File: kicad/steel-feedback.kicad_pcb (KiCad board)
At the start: 2 copper layers, 220 x 130 mm, 154 parts, among them J1 AudioJack2_SwitchT, J2 AudioJack2_SwitchT, J4 AudioJack2_SwitchT, J5 AudioJack2_SwitchT, J6 AudioJack2_SwitchT, J7 AudioJack2_SwitchT, J8 Jack-DC, Q1 2N3904, Q2 2N3906, Q3 2N3906, SW1 SW_SPDT, SW2 SW_SPDT, SW3 SW_SPDT, U10 TL072, U11 TL072, U12 TL072, U13 TL072, U2 LM13700, U3 LM13700, U4 TL072, U5 TL072, U6 LM386, U7 NE5534, U8 TL072, U9 ICL7660

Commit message: Tweaking values now that build is in progress
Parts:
- removed LS1: Speaker, KK254_Horizontal:Molex_KK-254_1x02_P2.54mm_Horizontal
- removed MK1: Piezo, KK254_Horizontal:Molex_KK-254_1x02_P2.54mm_Horizontal
- added H1: MountingHole_Pad, MountingHole:MountingHole_3.2mm_M3_Pad, F.Cu at (34.0, 34.0)
- added H2: MountingHole_Pad, MountingHole:MountingHole_3.2mm_M3_Pad, F.Cu at (246.0, 34.0)
- added H3: MountingHole_Pad, MountingHole:MountingHole_3.2mm_M3_Pad, F.Cu at (34.0, 156.0)
- added H4: MountingHole_Pad, MountingHole:MountingHole_3.2mm_M3_Pad, F.Cu at (246.0, 156.0)
- added J10: Conn_01x02, Rumblesan_Connectors:Molex_KK-254_22-05-7028_1x02_P2.54mm_Horizontal, F.Cu at (147.8, 139.7)
- added J3: Conn_01x03_Pin, Rumblesan_Connectors:Molex_KK-254_22-05-7038_1x03_P2.54mm_Horizontal, F.Cu at (215.1, 101.9)
- added J9: Conn_01x02, Rumblesan_Connectors:Molex_KK-254_22-05-7028_1x02_P2.54mm_Horizontal, F.Cu at (93.5, 139.8)
- C1, C2, C3: value 100pF -> 150pF
- C35: value 20pF -> 22pF
- C41: value 33nF -> 47nF
- C9: value 220uF -> 100uF
- J8: value Jack-DC -> Conn_01x02; footprint KK254_Horizontal:Molex_KK-254_1x02_P2.54mm_Horizontal -> Rumblesan_Connectors:Molex_KK-254_22-05-7028_1x02_P2.54mm_Horizontal
- R25: value 56k -> 68k
- R29: value 2k2 -> 2k
- moved C25 17.2 mm to (166.6, 133.9)
- moved C11 12.2 mm to (146.8, 113.5)
- moved C34 6.78 mm to (165.1, 145.8), turned to -90 degrees
- moved C9 6.61 mm to (86.9, 145.5), turned to 0 degrees
- moved C20 6.10 mm to (166.6, 138.7), turned to -90 degrees
- moved D3 5.24 mm to (180.1, 149.1)
- moved C10 3.81 mm to (141.7, 140.0)
- moved C7 1.80 mm to (83.3, 133.1)
- moved C29 1.78 mm to (196.8, 106.9), turned to 90 degrees
- moved J8 0.12 mm to (184.9, 140.0)
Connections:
- D3 pad 1: VCC -> Net-(D3-K)
- D3 pad 2: GND -> VCC
- SW1 pad 1: VCC -> Net-(D3-K)
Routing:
- net VEE: track 481.2 -> 496.3 mm
- net Net-(C11-Pad1): track 36.5 -> 48.7 mm
- net FEEDBACK_AUDIO: track 150.2 -> 139.5 mm
- net Net-(C41-Pad1): track 44.3 -> 52.5 mm
- net VCC: track 590.3 -> 597.7 mm, vias 0 -> 2
- net Net-(D3-K): track 0.00 -> 6.91 mm
- net Net-(U6-BYPASS): track 7.19 -> 9.07 mm
- net Net-(D1-A): track 47.8 -> 49.3 mm
- net Net-(C10-Pad1): track 5.50 -> 6.24 mm
- net GNDD: vias 1 -> 0
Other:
- board text added: "+V"
- board text added: "-V"
- board text added: "0V"
- board text added: "Debug Power"
- board text added: "Feedback Attenuvert"
- board text added: "Feedback CV"
- board text added: "Feedback Gain"
- board text added: "Frequency"
- board text added: "Frequency Attenuvert"
- board text added: "Frequency CV"
- board text added: "In Phase"
- board text added: "Input 1"
- board text added: "Input 2"
- board text added: "Invert"
- board text added: "Low Cut"
- board text added: "Off"
- board text added: "On"
- board text added: "Output 1"
- board text added: "Output 2"
- board text added: "Pickup"
- board text added: "Pickup Gain"
- board text added: "Plate Drive"
- board text added: "Resonance"

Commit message: Fixing issues in schematic
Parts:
- R18: value 10k -> 22k
- R25: value 68k -> 47k
- moved R47 10.3 mm to (128.1, 154.7)
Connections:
- J10 pad 1: VEE -> GND
- R47 pad 1: VCC -> Net-(D1-A)
- R47 pad 2: Net-(D1-A) -> GND
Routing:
- net VEE: track 496.3 -> 485.4 mm
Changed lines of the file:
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@@
 			)
 		)
-		(property "Value" "10k"
+		(property "Value" "22k"
 			(at 8.128 0.6 90)
 			(layer "F.Fab")
@@
 			(layers "*.Cu" "*.Mask")
 			(remove_unused_layers no)
-			(net 17 "VEE")
+			(net 10 "GND")
 			(pinfunction "Pin_1")
 			(pintype "passive")
@@
 	(footprint "Rumblesan_Standard_Parts:R_Axial_DIN0207_L6.3mm_D2.5mm_P10.16mm_Horizontal"
 		(layer "F.Cu")
-		(at 117.856 154.686)
+		(at 128.143 154.686)
 		(descr "Resistor, Axial_DIN0207 series, Axial, Horizontal, pin pitch=10.16mm, 0.25W = 1/4W, length*diameter=6.3*2.5mm^2, http://cdn-reichelt.de/documents/datenblatt/B400/1_4W%23YAG.pdf")
 		(tags "Resistor Axial_DIN0207 series Axial Horizontal pin pitch 10.16mm 0.25W = 1/4W length 6.3mm diameter 2.5mm")
@@
 			(layers "*.Cu" "*.Mask")
 			(remove_unused_layers no)
-			(net 16 "VCC")
+			(net 21 "Net-(D1-A)")
 			(pintype "passive")
 		)
@@
 			(layers "*.Cu" "*.Mask")
 			(remove_unused_layers no)
-			(net 21 "Net-(D1-A)")
+			(net 10 "GND")
 			(pintype "passive")
 		)
@@
 			)
 		)
-		(property "Value" "68k"
+		(property "Value" "47k"
 			(at 8.128 0.6 0)
 			(layer "F.Fab")
@@
 	)
 	(segment
-		(start 147.828 143.256)
-		(end 146.558 143.256)
+		(start 190.246 135.636)
+		(end 192.532 133.35)
 		(width 0.635)
 		(layer "B.Cu")
@@
 	)
 	(segment
-		(start 146.558 143.256)
-		(end 151.384 143.256)
+		(start 144.272 67.056)
+		(end 154.686 67.056)
 		(width 0.635)
 		(layer "B.Cu")
@@
 	)
 	(segment
-		(start 144.272 67.056)
-		(end 154.686 67.056)
+		(start 190.246 153.67)
+		(end 190.246 135.636)
 		(width 0.635)
 		(layer "B.Cu")
@@
 	)
 	(segment
-		(start 141.986 78.212)
-		(end 141.986 69.342)
+		(start 153.797 151.384)
+		(end 156.845 154.432)
 		(width 0.635)
 		(layer "B.Cu")
@@
 	)
 	(segment
-		(start 147.828 139.7)
-		(end 147.828 143.256)
+		(start 189.484 154.432)
+		(end 190.246 153.67)
+		(width 0.635)
+		(layer "B.Cu")
+		(net 17)
+	)
+	(segment
+		(start 141.986 78.212)
+		(end 141.986 69.342)
 		(width 0.635)
 		(layer "B.Cu")
@@
 	)
 	(segment
-		(start 186.69 157.226)
-		(end 190.246 153.67)
+		(start 156.845 154.432)
+		(end 189.484 154.432)
 		(width 0.635)
 		(layer "B.Cu")
@@
 	)
 	(segment
-		(start 136.398 147.828)
-		(end 136.398 147.32)
-		(width 0.635)
-		(layer "B.Cu")
-		(net 17)
-	)
-	(segment
-		(start 140.462 147.828)
-		(end 145.034 143.256)
+		(start 141.986 147.828)
+		(end 145.542 151.384)
 		(width 0.635)
 		(layer "B.Cu")
@@
 	)
 	(segment
-		(start 145.034 143.256)
-		(end 146.558 143.256)
+		(start 136.398 147.828)
+		(end 136.398 147.32)
 		(width 0.635)
 		(layer "B.Cu")
@@
 	)
 	(segment
-		(start 136.398 147.828)
-		(end 140.462 147.828)
+		(start 145.542 151.384)
+		(end 153.797 151.384)
 		(width 0.635)
 		(layer "B.Cu")
@@
 	)
 	(segment
-		(start 151.384 143.256)
-		(end 165.354 157.226)
-		(width 0.635)
-		(layer "B.Cu")
-		(net 17)
-	)
-	(segment
-		(start 190.246 153.67)
-		(end 190.246 135.636)
-		(width 0.635)
-		(layer "B.Cu")
-		(net 17)
-	)
-	(segment
-		(start 190.246 135.636)
-		(end 192.532 133.35)
-		(width 0.635)
-		(layer "B.Cu")
-		(net 17)
-	)
-	(segment
-		(start 165.354 157.226)
-		(end 186.69 157.226)
+		(start 141.986 69.342)
+		(end 144.272 67.056)
 		(width 0.635)
 		(layer "B.Cu")
@@
 	)
 	(segment
-		(start 141.986 69.342)
-		(end 144.272 67.056)
+		(start 136.398 147.828)
+		(end 141.986 147.828)
 		(width 0.635)
 		(layer "B.Cu")

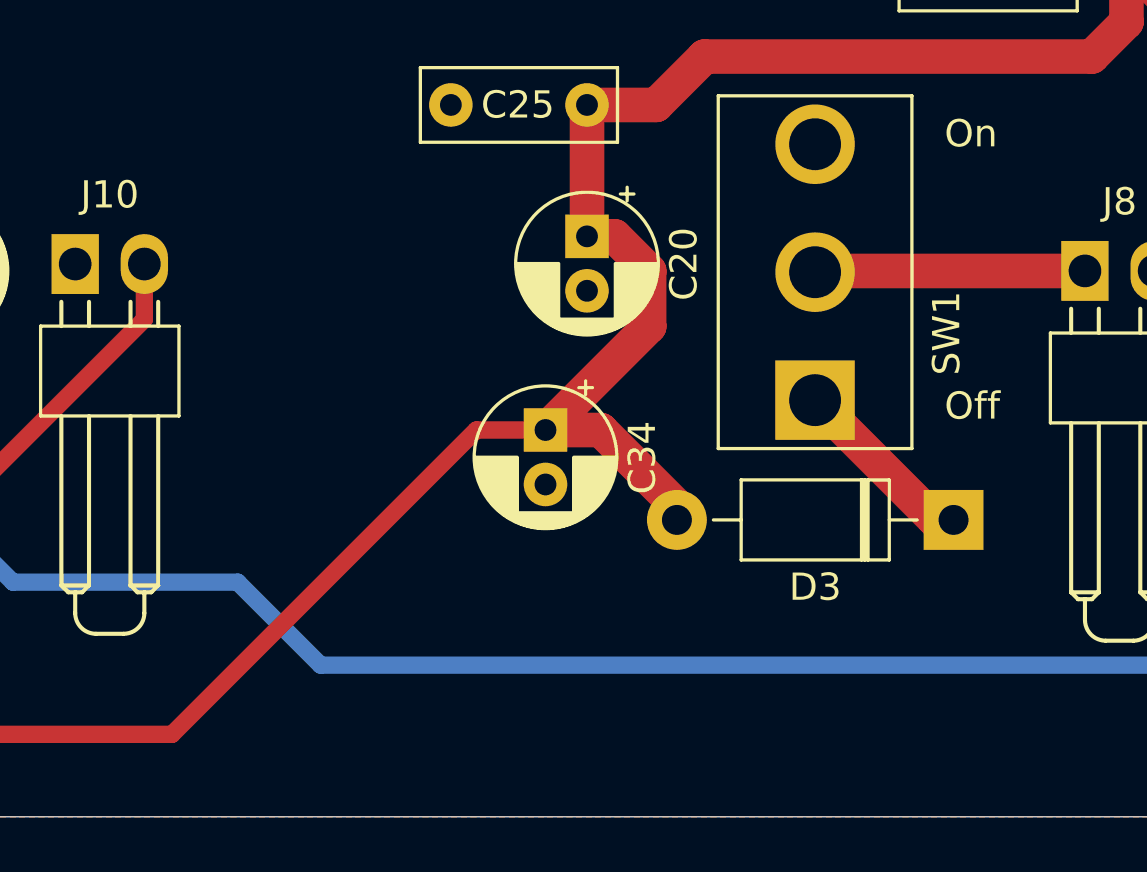
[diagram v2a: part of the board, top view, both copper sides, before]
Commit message: Fixing issues with power circuitry
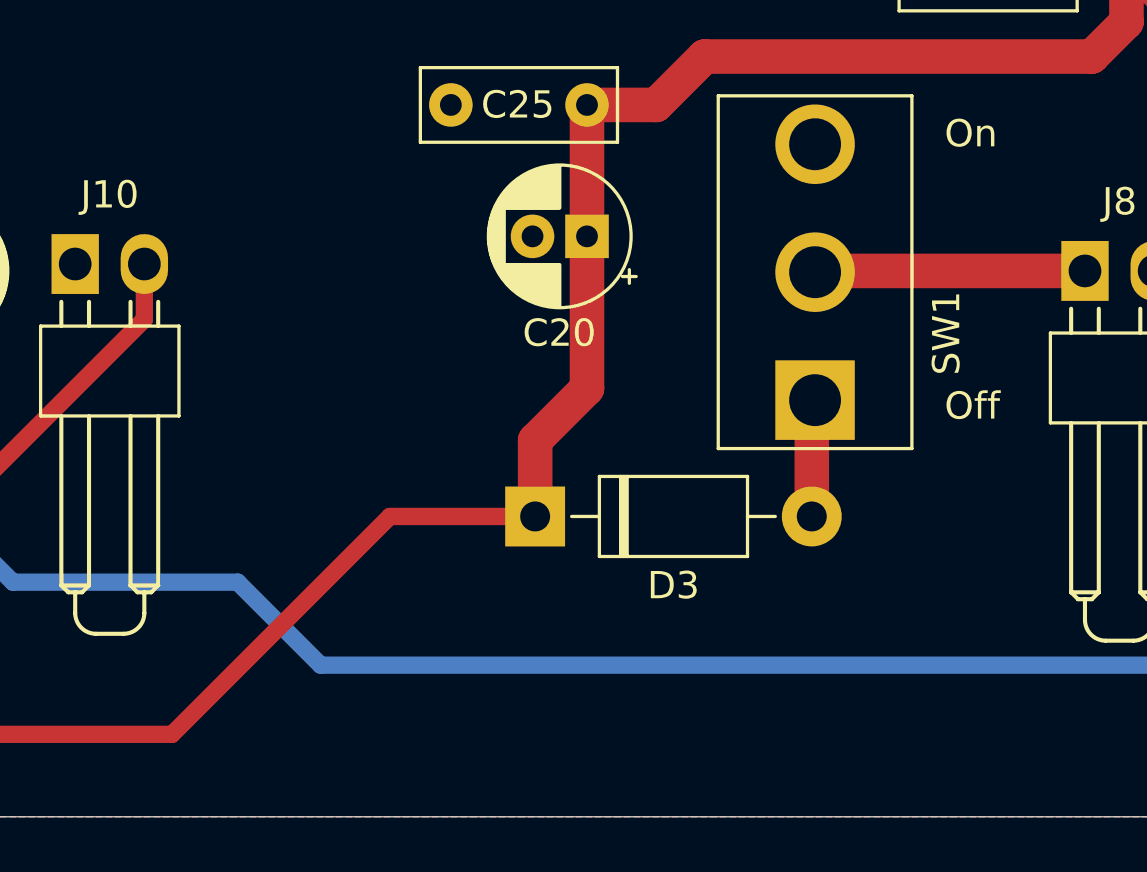
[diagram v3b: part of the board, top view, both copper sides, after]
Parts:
- removed C34: 10uF, Rumblesan_Standard_Parts:CP_Radial_D5.0mm_P2.00mm
- C20: value 10uF -> 22uF
- moved D3 15.4 mm to (164.7, 149.0), turned to 0 degrees
- turned C20 to 180 degrees
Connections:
- D3 pad 1: Net-(D3-K) -> VCC
- D3 pad 2: VCC -> Net-(D3-A)
- SW1 pad 1: Net-(D3-K) -> Net-(D3-A)
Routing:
- net VCC: track 597.7 -> 590.3 mm
- net Net-(D3-K): track 6.91 -> 0.00 mm
- net Net-(D3-A): track 0.00 -> 4.32 mm
